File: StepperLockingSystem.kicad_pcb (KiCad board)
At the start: 4 copper layers, 54 x 84 mm, 106 parts, among them J1 Nerdstern, J10 MotorNTC, J11 Stepper, J12 HallEncoder, J2 DigitalLED, J3 Open+Close, J4 SWD, J5 6Pin DuPont 2.56mm, J6 5Pin DuPont 2.54mm, J7 LockState, J8 DoorState, J9 PowerConnector, Q1 IRLML0030, SW1 Reset, U1 STM32G0B1KET, U2 24LC64, U3 TC1185, U4 INA180A1, U5 USBLC6-2SC6, U6 USBLC6-2SC6, U7 TMC2209-LA, Y1 ABM3B-16MHz

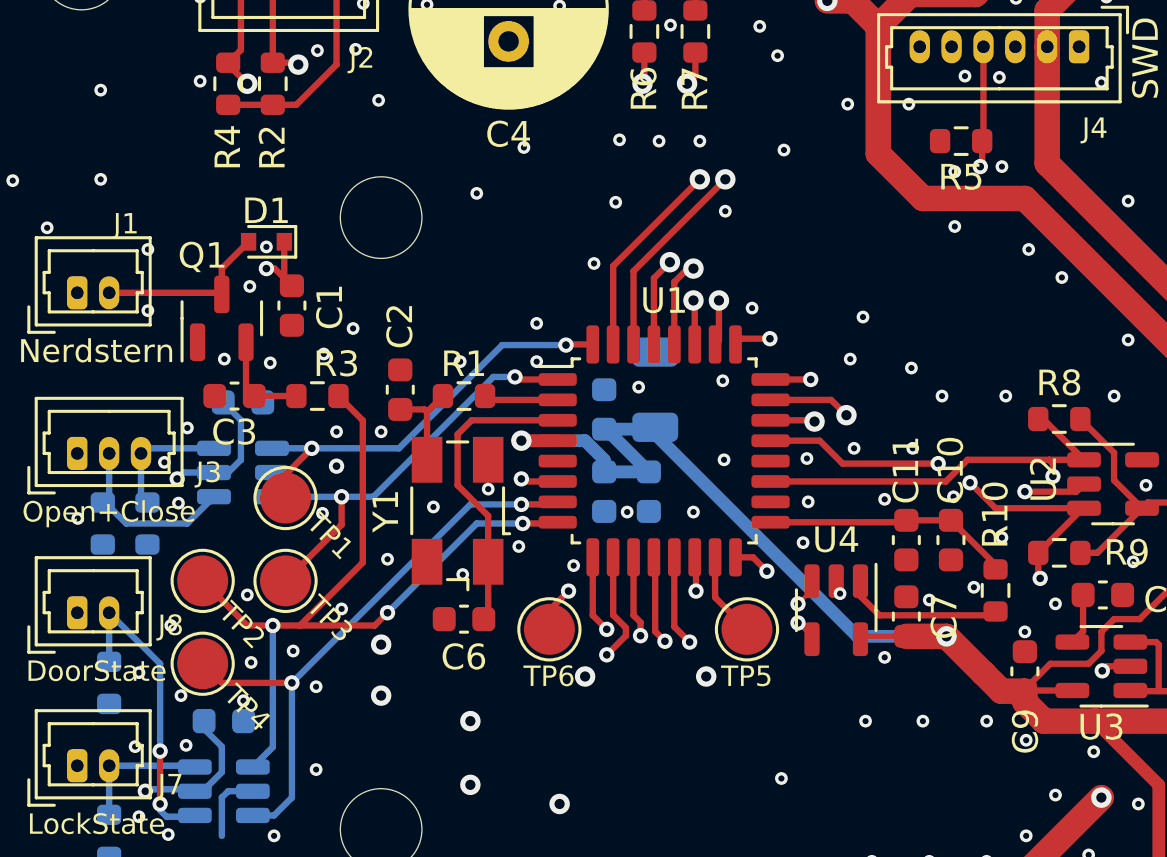
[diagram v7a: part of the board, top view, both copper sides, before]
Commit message: Update footprint and export step file
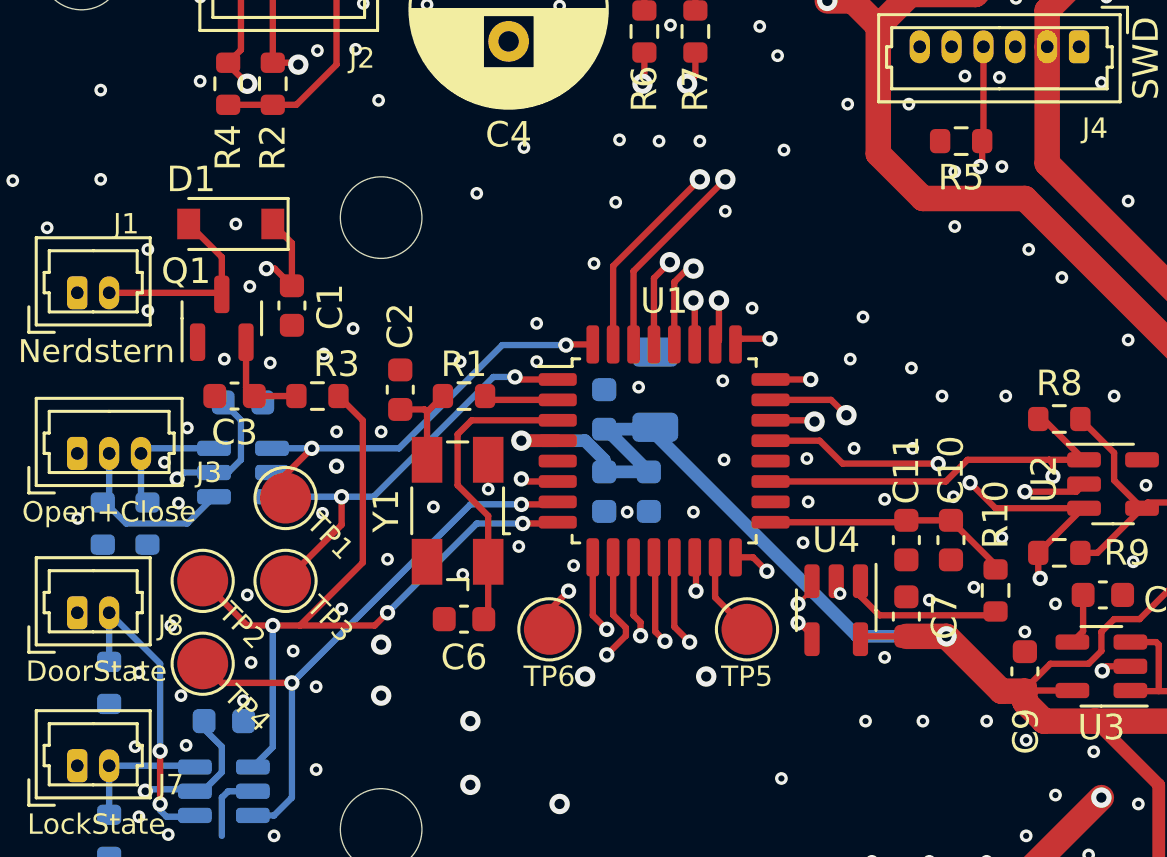
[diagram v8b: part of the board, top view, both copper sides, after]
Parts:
- D1: value D_Schottky -> BAT54WHE3-TP; footprint Diode_SMD:D_SOD-523 -> Diode_SMD:D_SOD-123
- moved D1 1.57 mm to (129.8, 77.3)
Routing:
- net VCC: track 161.1 -> 162.0 mm
- net Net-(D1-Pad2): track 6.94 -> 7.75 mm
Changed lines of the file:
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@@
     )
   )
-  (footprint "Diode_SMD:D_SOD-523" (layer "F.Cu")
-    (at 131.25 78.05 180)
-    (descr "http://www.diodes.com/datasheets/ap02001.pdf p.144")
-    (tags "Diode SOD523")
+  (footprint "Diode_SMD:D_SOD-123" (layer "F.Cu")
+    (at 129.85 77.35 180)
+    (descr "SOD-123")
+    (tags "SOD-123")
     (property "Sheetfile" "mcu.kicad_sch")
     (property "Sheetname" "MCU")
     (attr smd)
-    (fp_text reference "D1" (at 0 1.2) (layer "F.SilkS")
+    (fp_text reference "D1" (at 1.55 1.75 180) (layer "F.SilkS")
       (effects (font (size 1 1) (thickness 0.15)))
     )
-    (fp_text value "D_Schottky" (at 0 1.4) (layer "F.Fab")
+    (fp_text value "BAT54WHE3-TP" (at 0 2.1 180) (layer "F.Fab")
       (effects (font (size 1 1) (thickness 0.15)))
     )
-    (fp_text user "${REFERENCE}" (at 0 -1.3) (layer "F.Fab")
+    (fp_text user "${REFERENCE}" (at 0 -2 180) (layer "F.Fab")
       (effects (font (size 1 1) (thickness 0.15)))
     )
-    (fp_line (start 0.7 -0.6) (end -1.15 -0.6) (layer "F.SilkS") (width 0.12))
-    (fp_line (start 0.7 0.6) (end -1.15 0.6) (layer "F.SilkS") (width 0.12))
-    (fp_line (start -1.15 -0.6) (end -1.15 0.6) (layer "F.SilkS") (width 0.12))
-    (fp_line (start -1.25 0.7) (end -1.25 -0.7) (layer "F.CrtYd") (width 0.05))
-    (fp_line (start 1.25 -0.7) (end 1.25 0.7) (layer "F.CrtYd") (width 0.05))
-    (fp_line (start -1.25 -0.7) (end 1.25 -0.7) (layer "F.CrtYd") (width 0.05))
-    (fp_line (start 1.25 0.7) (end -1.25 0.7) (layer "F.CrtYd") (width 0.05))
-    (fp_line (start 0.65 0.45) (end -0.65 0.45) (layer "F.Fab") (width 0.1))
-    (fp_line (start 0.1 0.2) (end 0.1 -0.2) (layer "F.Fab") (width 0.1))
-    (fp_line (start -0.2 0.2) (end -0.2 -0.2) (layer "F.Fab") (width 0.1))
-    (fp_line (start 0.1 0) (end 0.25 0) (layer "F.Fab") (width 0.1))
-    (fp_line (start 0.65 -0.45) (end 0.65 0.45) (layer "F.Fab") (width 0.1))
-    (fp_line (start -0.2 0) (end -0.35 0) (layer "F.Fab") (width 0.1))
-    (fp_line (start 0.1 -0.2) (end -0.2 0) (layer "F.Fab") (width 0.1))
-    (fp_line (start -0.2 0) (end 0.1 0.2) (layer "F.Fab") (width 0.1))
-    (fp_line (start -0.65 0.45) (end -0.65 -0.45) (layer "F.Fab") (width 0.1))
-    (fp_line (start -0.65 -0.45) (end 0.65 -0.45) (layer "F.Fab") (width 0.1))
-    (pad "1" smd rect (at -0.7 0) (size 0.6 0.7) (layers "F.Cu" "F.Paste" "F.Mask")
+    (fp_line (start -2.25 1) (end 1.65 1) (layer "F.SilkS") (width 0.12))
+    (fp_line (start -2.25 -1) (end -2.25 1) (layer "F.SilkS") (width 0.12))
+    (fp_line (start -2.25 -1) (end 1.65 -1) (layer "F.SilkS") (width 0.12))
+    (fp_line (start -2.35 -1.15) (end 2.35 -1.15) (layer "F.CrtYd") (width 0.05))
+    (fp_line (start -2.35 -1.15) (end -2.35 1.15) (layer "F.CrtYd") (width 0.05))
+    (fp_line (start 2.35 -1.15) (end 2.35 1.15) (layer "F.CrtYd") (width 0.05))
+    (fp_line (start 2.35 1.15) (end -2.35 1.15) (layer "F.CrtYd") (width 0.05))
+    (fp_line (start 1.4 -0.9) (end 1.4 0.9) (layer "F.Fab") (width 0.1))
+    (fp_line (start 0.25 0.4) (end -0.35 0) (layer "F.Fab") (width 0.1))
+    (fp_line (start 0.25 0) (end 0.75 0) (layer "F.Fab") (width 0.1))
+    (fp_line (start 1.4 0.9) (end -1.4 0.9) (layer "F.Fab") (width 0.1))
+    (fp_line (start -0.35 0) (end 0.25 -0.4) (layer "F.Fab") (width 0.1))
+    (fp_line (start 0.25 -0.4) (end 0.25 0.4) (layer "F.Fab") (width 0.1))
+    (fp_line (start -1.4 -0.9) (end 1.4 -0.9) (layer "F.Fab") (width 0.1))
+    (fp_line (start -0.75 0) (end -0.35 0) (layer "F.Fab") (width 0.1))
+    (fp_line (start -0.35 0) (end -0.35 -0.55) (layer "F.Fab") (width 0.1))
+    (fp_line (start -0.35 0) (end -0.35 0.55) (layer "F.Fab") (width 0.1))
+    (fp_line (start -1.4 0.9) (end -1.4 -0.9) (layer "F.Fab") (width 0.1))
+    (pad "1" smd rect (at -1.65 0 180) (size 0.9 1.2) (layers "F.Cu" "F.Paste" "F.Mask")
       (net 4 "VCC") (pinfunction "K") (pintype "passive"))
-    (pad "2" smd rect (at 0.7 0) (size 0.6 0.7) (layers "F.Cu" "F.Paste" "F.Mask")
+    (pad "2" smd rect (at 1.65 0 180) (size 0.9 1.2) (layers "F.Cu" "F.Paste" "F.Mask")
       (net 46 "Net-(D1-Pad2)") (pinfunction "A") (pintype "passive"))
-    (model "${KICAD6_3DMODEL_DIR}/Diode_SMD.3dshapes/D_SOD-523.wrl"
+    (model "${KICAD6_3DMODEL_DIR}/Diode_SMD.3dshapes/D_SOD-123.wrl"
       (offset (xyz 0 0 0))
       (scale (xyz 1 1 1))
@@
     (property "Sheetname" "MCU")
     (attr smd)
-    (fp_text reference "Q1" (at 2.45 -0.75 180) (layer "F.SilkS")
+    (fp_text reference "Q1" (at 1.85 -1.4 180) (layer "F.SilkS")
       (effects (font (size 1 1) (thickness 0.15)))
     )
@@
   (via (at 161 93.35) (size 0.5) (drill 0.24) (layers "F.Cu" "B.Cu") (free) (net 1))
   (via (at 128.15 85.35) (size 0.5) (drill 0.24) (layers "F.Cu" "B.Cu") (free) (net 1))
-  (via (at 131.25 78.25) (size 0.5) (drill 0.24) (layers "F.Cu" "B.Cu") (free) (net 1))
+  (via (at 130.05 77.35) (size 0.5) (drill 0.24) (layers "F.Cu" "B.Cu") (free) (net 1))
   (via (at 152.45 86.55) (size 0.5) (drill 0.24) (layers "F.Cu" "B.Cu") (free) (net 1))
   (via (at 163 115.35) (size 0.5) (drill 0.24) (layers "F.Cu" "B.Cu") (free) (net 1))
@@
   (segment (start 163.5 94.6) (end 164 94.1) (width 0.25) (layer "F.Cu") (net 2))
   (segment (start 162 94.6) (end 163.5 94.6) (width 0.25) (layer "F.Cu") (net 2))
-  (segment (start 160.075 95.675) (end 159.375 94.975) (width 1) (layer "F.Cu") (net 2))
+  (segment (start 157.925 93.525) (end 160.075 95.675) (width 1) (layer "F.Cu") (net 2))
   (segment (start 170.925 84.025) (end 161.875 74.975) (width 1) (layer "F.Cu") (net 2))
   (segment (start 162 145.1) (end 167.755692 145.1) (width 0.5) (layer "F.Cu") (net 2))
   (segment (start 167.35 91) (end 165.5 92.85) (width 0.25) (layer "F.Cu") (net 2))
   (segment (start 155.25 131.6) (end 155.25 134.6) (width 0.25) (layer "F.Cu") (net 2))
-  (segment (start 159.375 94.975) (end 157.925 93.525) (width 1) (layer "F.Cu") (net 2))
   (segment (start 161 95.675) (end 160.075 95.675) (width 1) (layer "F.Cu") (net 2))
   (segment (start 173.5 95.35) (end 173.5 86.525) (width 1) (layer "F.Cu") (net 2))
@@
   (segment (start 131.575 79.1) (end 132.25 79.775) (width 0.25) (layer "F.Cu") (net 4))
   (segment (start 152.65 93.549503) (end 152.1 92.999503) (width 0.15) (layer "F.Cu") (net 4))
+  (segment (start 132.25 79.775) (end 132.25 78.1) (width 0.25) (layer "F.Cu") (net 4))
   (segment (start 164 120.35) (end 162 120.35) (width 0.15) (layer "F.Cu") (net 4))
-  (segment (start 131.95 78.05) (end 131.95 79.475) (width 0.25) (layer "F.Cu") (net 4))
+  (segment (start 132.25 78.1) (end 131.5 77.35) (width 0.25) (layer "F.Cu") (net 4))
   (segment (start 152.65 93.6375) (end 152.65 93.549503) (width 0.15) (layer "F.Cu") (net 4))
-  (segment (start 131.95 79.475) (end 132.25 79.775) (width 0.25) (layer "F.Cu") (net 4))
   (segment (start 131.25 79.1) (end 131.575 79.1) (width 0.25) (layer "F.Cu") (net 4))
   (segment (start 160 120.35) (end 159.75 120.1) (width 0.25) (layer "F.Cu") (net 4))
@@
   (segment (start 129.4375 80.05) (end 129.5 80.1125) (width 0.25) (layer "F.Cu") (net 46))
   (segment (start 125.08125 80.05) (end 129.4375 80.05) (width 0.25) (layer "F.Cu") (net 46))
-  (segment (start 129.5 79.1) (end 130.55 78.05) (width 0.25) (layer "F.Cu") (net 46))
-  (segment (start 129.5 80.1125) (end 129.5 79.1) (width 0.25) (layer "F.Cu") (net 46))
+  (segment (start 128.2 77.35) (end 129.5 78.65) (width 0.25) (layer "F.Cu") (net 46))
+  (segment (start 129.5 78.65) (end 129.5 80.1125) (width 0.25) (layer "F.Cu") (net 46))
   (segment (start 148.075 67.85) (end 147.5 67.275) (width 0.25) (layer "F.Cu") (net 47))
   (segment (start 148.075 68.975) (end 148.075 67.85) (width 0.25) (layer "F.Cu") (net 47))
